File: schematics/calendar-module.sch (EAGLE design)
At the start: 175 parts

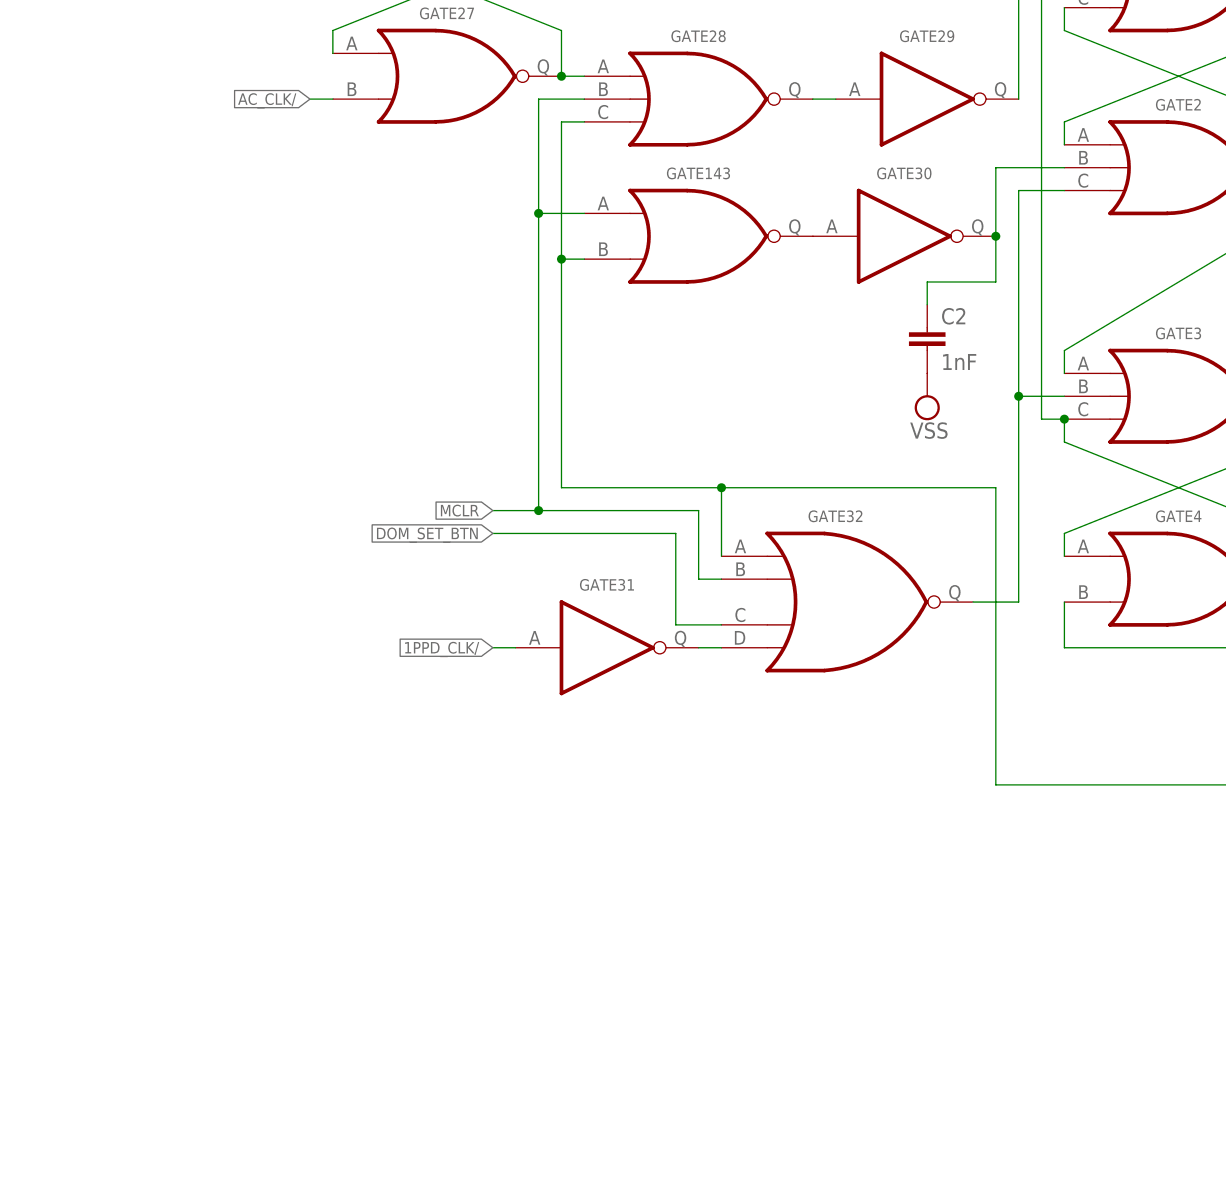
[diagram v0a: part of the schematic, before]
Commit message: Calendar module schematics (#14)
* Add revised calendar module schematics
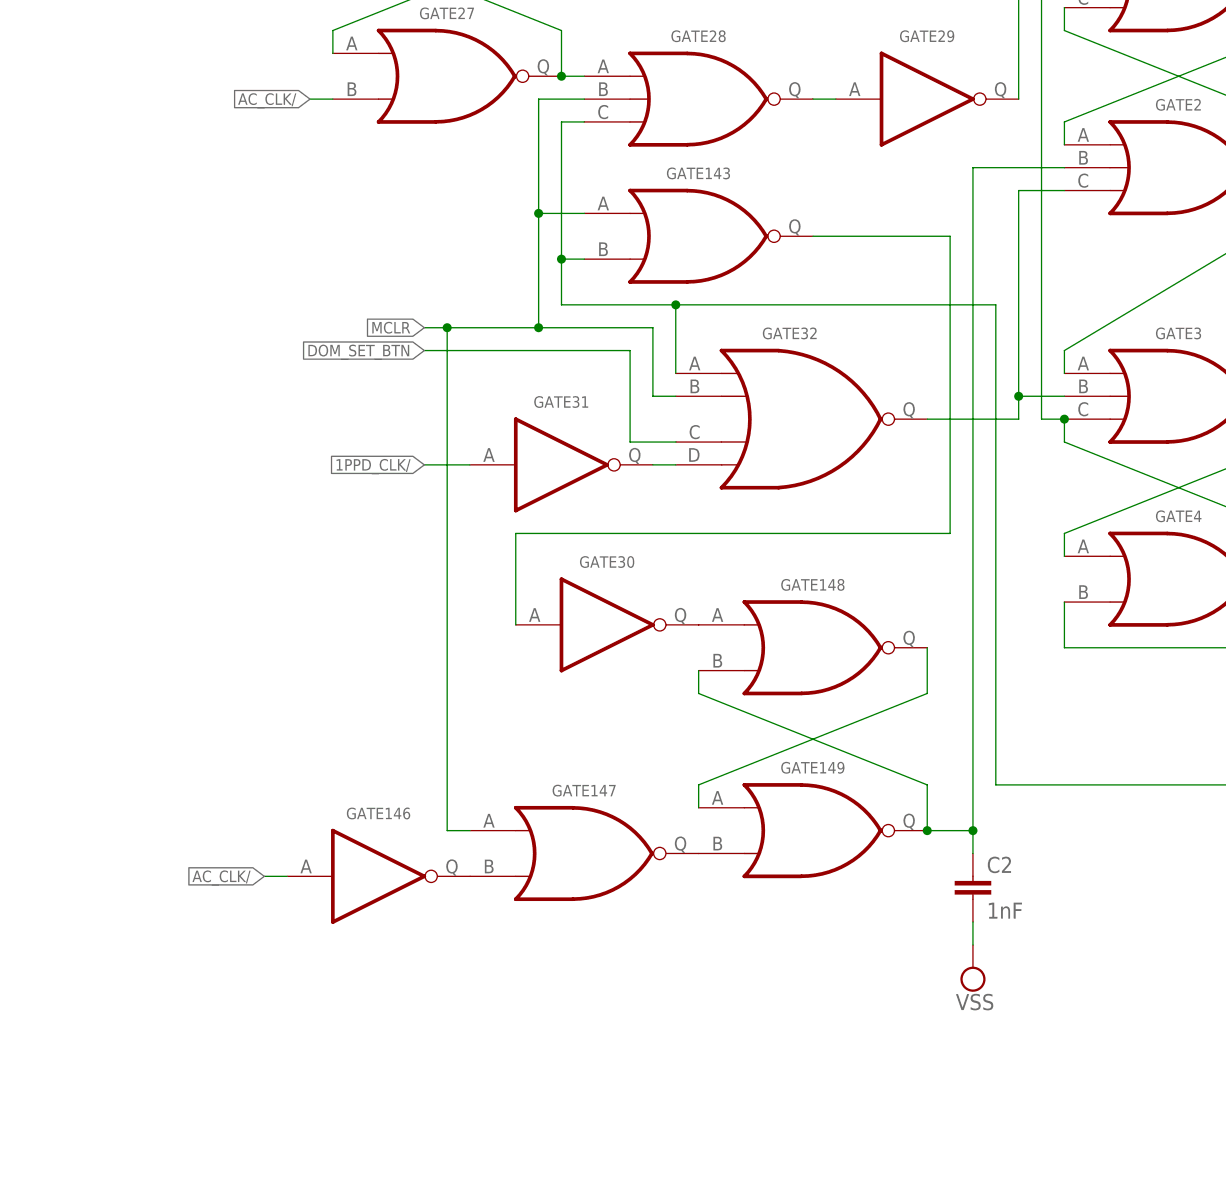
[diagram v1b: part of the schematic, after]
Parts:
- added GATE146: INVERTER, NOR gate clock:INVERTER
- added GATE147, GATE148, GATE149: 2NOR, NOR gate clock:2NOR
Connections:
- new net N$38: GATE146.Q, GATE147.B
- new net N$57: GATE148.Q, GATE149.A
- new net N$62: C2.1, GATE148.B, GATE149.Q, GATE2.B
- new net N$76: GATE147.Q, GATE149.B
- net AC_CLK/: now also GATE146.A
- net DOM_SET_BTN: now also GATE32.C
- net MCLR: now also GATE147.A
- net N$117: now also GATE148.A; no longer C2.1, GATE2.B
- net N$47: now also GATE32.D
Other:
- moved on the sheet: C2, GATE30, GATE31, GATE32

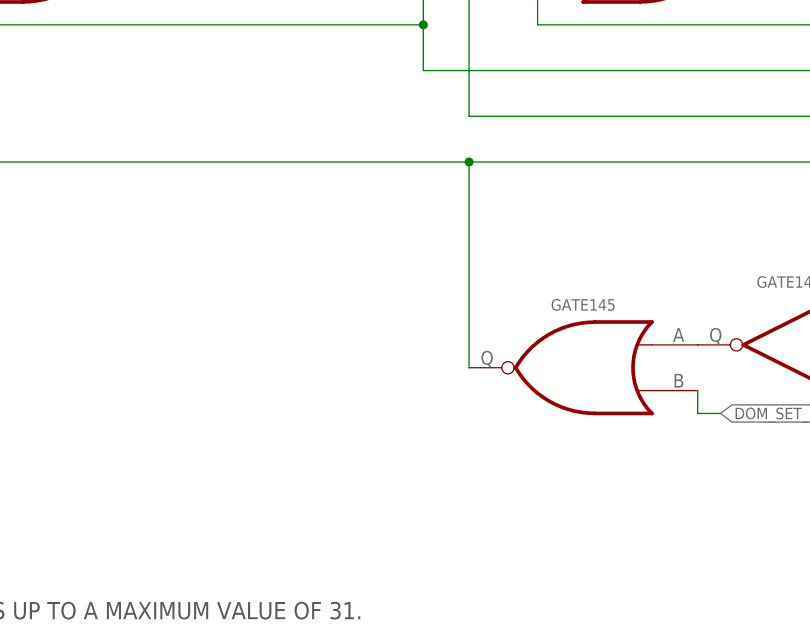
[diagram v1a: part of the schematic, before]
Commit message: Upload new calendar module schematic.
Fixes rollover bug which caused calendar module to roll over from 29th day of a month to day 00 of the next month.
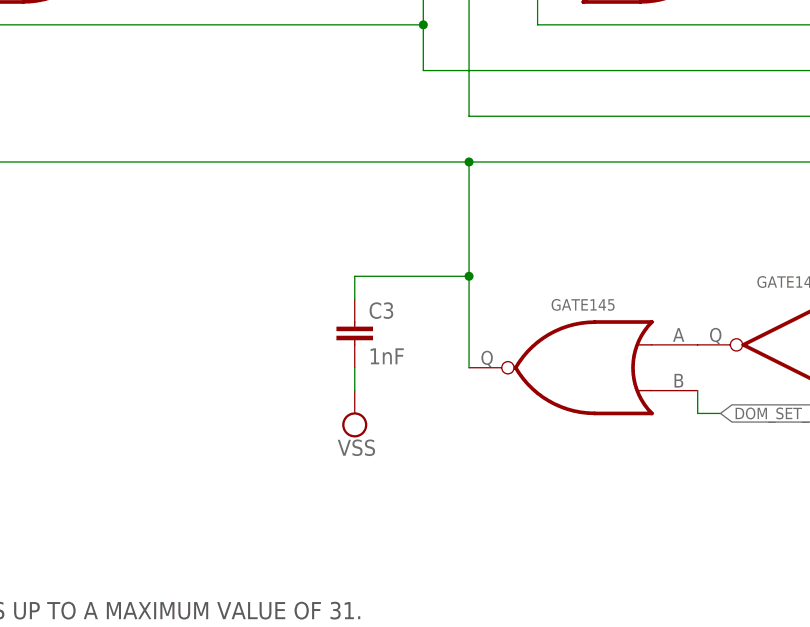
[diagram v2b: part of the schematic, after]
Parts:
- added C3: 1nF, rcl:C-EU050-025X075
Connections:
- net DOM_RESET: now also C3.1
- net VSS: now also C3.2
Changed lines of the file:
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@@
 <part name="GATE148" library="NOR gate clock" deviceset="2NOR" device=""/>
 <part name="GATE149" library="NOR gate clock" deviceset="2NOR" device=""/>
+<part name="C3" library="rcl" deviceset="C-EU" device="050-025X075" value="1nF"/>
+<part name="SUPPLY22" library="supply2" deviceset="VSS" device=""/>
 </parts>
 <sheets>
@@
 <instance part="GATE148" gate="G$1" x="106.68" y="431.8"/>
 <instance part="GATE149" gate="G$1" x="106.68" y="411.48"/>
+<instance part="C3" gate="G$1" x="182.88" y="398.78"/>
+<instance part="SUPPLY22" gate="G$1" x="182.88" y="388.62"/>
 </instances>
 <busses>
@@
 <pinref part="GATE145" gate="G$1" pin="Q"/>
 <wire x1="406.4" y1="482.6" x2="406.4" y2="416.56" width="0.1524" layer="91"/>
-<wire x1="195.58" y1="393.7" x2="195.58" y2="416.56" width="0.1524" layer="91"/>
+<wire x1="195.58" y1="393.7" x2="195.58" y2="403.86" width="0.1524" layer="91"/>
+<wire x1="195.58" y1="403.86" x2="195.58" y2="416.56" width="0.1524" layer="91"/>
 <wire x1="195.58" y1="416.56" x2="127" y2="416.56" width="0.1524" layer="91"/>
 <wire x1="127" y1="416.56" x2="127" y2="469.9" width="0.1524" layer="91"/>
@@
 <wire x1="91.44" y1="462.28" x2="91.44" y2="469.9" width="0.1524" layer="91"/>
 <junction x="91.44" y="469.9"/>
+<pinref part="C3" gate="G$1" pin="1"/>
+<wire x1="195.58" y1="403.86" x2="182.88" y2="403.86" width="0.1524" layer="91"/>
+<wire x1="182.88" y1="403.86" x2="182.88" y2="401.32" width="0.1524" layer="91"/>
+<junction x="195.58" y="403.86"/>
 </segment>
 </net>
@@
 <wire x1="124.46" y1="401.32" x2="124.46" y2="398.78" width="0.1524" layer="91"/>
 </segment>
-</net>
+<segment>
+<pinref part="SUPPLY22" gate="G$1" pin="VSS"/>
+<pinref part="C3" gate="G$1" pin="2"/>
+<wire x1="182.88" y1="391.16" x2="182.88" y2="393.7" width="0.1524" layer="91"/>
+</segment>
+</net>
